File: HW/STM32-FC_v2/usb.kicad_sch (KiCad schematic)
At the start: 33 parts, among them J2 USB_C_USB2.0_14P, J3 GH 1.25mm 6P, Q2 PMDPB30XN, Q3 PMDPB55XP, U2 USBLC6-2SC6, U3 TPS62840, U4 TPS62840, U5 TPS62840

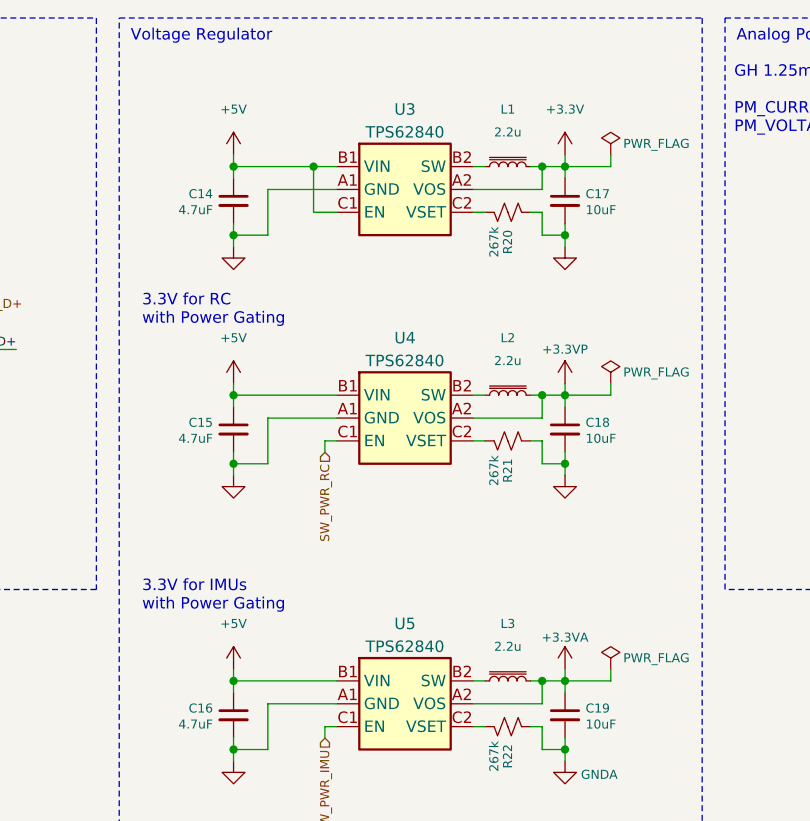
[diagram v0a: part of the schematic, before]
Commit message: bug fix about servo output
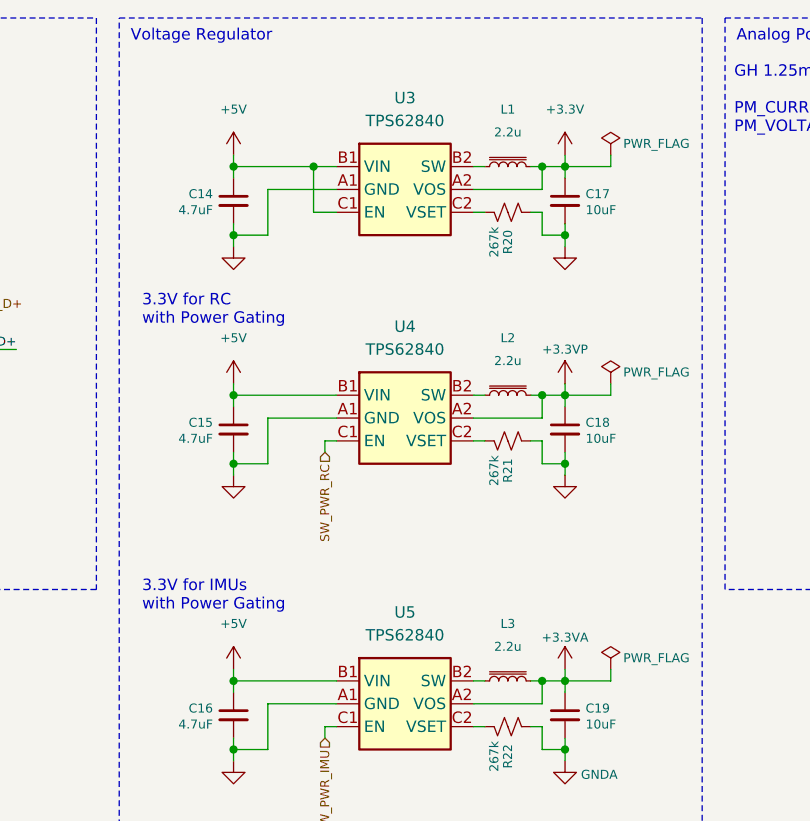
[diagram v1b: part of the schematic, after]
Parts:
- U3, U4, U5: symbol TPS62840YBG:TPS62840YBG -> TPS62840:TPS62840YBG
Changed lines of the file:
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@@
 	)
 	(symbol
-		(lib_id "TPS62840YBG:TPS62840YBG")
+		(lib_id "TPS62840:TPS62840YBG")
 		(at 170.18 31.75 0)
 		(unit 1)
@@
 		(fields_autoplaced yes)
 		(property "Reference" "U3"
-			(at 170.18 22.86 0)
+			(at 170.18 21.59 0)
 			(effects
 				(font
@@
 		)
 		(property "Value" "TPS62840"
-			(at 170.18 25.4 0)
+			(at 170.18 24.13 0)
 			(effects
 				(font
@@
 			)
 		)
-		(property "Datasheet" ""
+		(property "Datasheet" "https://www.ti.com/lit/ds/symlink/tps62840.pdf"
 			(at 170.18 31.75 0)
 			(effects
@@
 			)
 		)
-		(property "Description" ""
+		(property "Description" "VIN 1.8-V to 6.5-V, VOUT 1.8 V to 3.3 V in 100-mV steps, 750-mA, 60-nA IQ Step-Down Converter"
 			(at 170.18 31.75 0)
 			(effects
@@
 	)
 	(symbol
-		(lib_id "TPS62840YBG:TPS62840YBG")
+		(lib_id "TPS62840:TPS62840YBG")
 		(at 170.18 57.15 0)
 		(unit 1)
@@
 		(fields_autoplaced yes)
 		(property "Reference" "U4"
-			(at 170.18 48.26 0)
+			(at 170.18 46.99 0)
 			(effects
 				(font
@@
 		)
 		(property "Value" "TPS62840"
-			(at 170.18 50.8 0)
+			(at 170.18 49.53 0)
 			(effects
 				(font
@@
 			)
 		)
-		(property "Datasheet" ""
+		(property "Datasheet" "https://www.ti.com/lit/ds/symlink/tps62840.pdf"
 			(at 170.18 57.15 0)
 			(effects
@@
 			)
 		)
-		(property "Description" ""
+		(property "Description" "VIN 1.8-V to 6.5-V, VOUT 1.8 V to 3.3 V in 100-mV steps, 750-mA, 60-nA IQ Step-Down Converter"
 			(at 170.18 57.15 0)
 			(effects
@@
 	)
 	(symbol
-		(lib_id "TPS62840YBG:TPS62840YBG")
+		(lib_id "TPS62840:TPS62840YBG")
 		(at 170.18 88.9 0)
 		(unit 1)
@@
 		(fields_autoplaced yes)
 		(property "Reference" "U5"
-			(at 170.18 80.01 0)
+			(at 170.18 78.74 0)
 			(effects
 				(font
@@
 		)
 		(property "Value" "TPS62840"
-			(at 170.18 82.55 0)
+			(at 170.18 81.28 0)
 			(effects
 				(font
@@
 			)
 		)
-		(property "Datasheet" ""
+		(property "Datasheet" "https://www.ti.com/lit/ds/symlink/tps62840.pdf"
 			(at 170.18 88.9 0)
 			(effects
@@
 			)
 		)
-		(property "Description" ""
+		(property "Description" "VIN 1.8-V to 6.5-V, VOUT 1.8 V to 3.3 V in 100-mV steps, 750-mA, 60-nA IQ Step-Down Converter"
 			(at 170.18 88.9 0)
 			(effects
